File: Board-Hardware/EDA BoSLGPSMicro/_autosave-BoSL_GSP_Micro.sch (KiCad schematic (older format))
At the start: 45 parts, among them CON1 Micro_SD_Card, CON2 BARREL_JACK, IC2 SIM7000, J7 USB_B_Micro, P2 CONN_01X04, P4 CONN_01X04, P7 CONN_01X04, SW1 SPST, U1 MCP1700T-3302E/TT, U2 ATmega328P-AU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

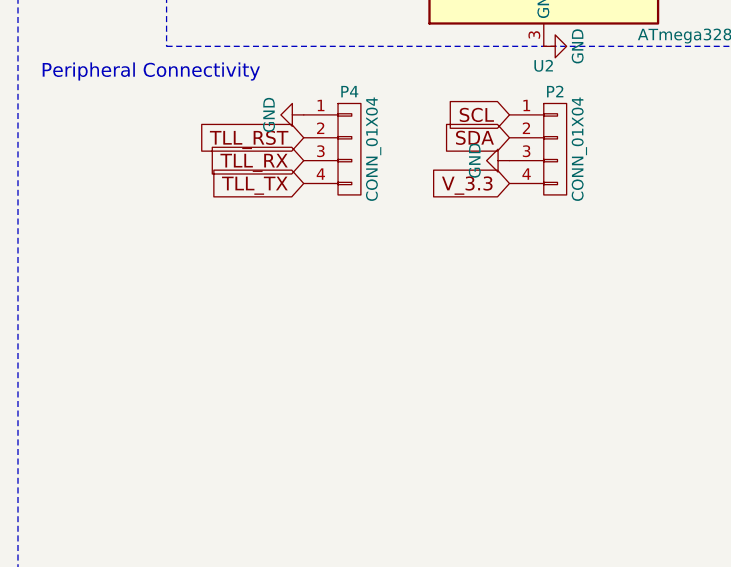
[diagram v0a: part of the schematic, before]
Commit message: added spi header to bosl GPS micro for bootloading
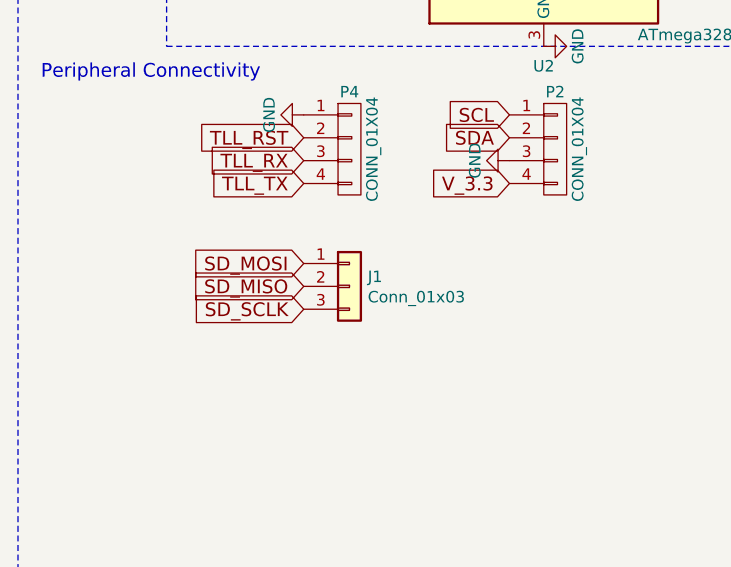
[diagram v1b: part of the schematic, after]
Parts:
- added J1: Conn_01x03, Pin_Headers:Pin_Header_Straight_1x03_Pitch2.54mm, symbol Connector_Generic:Conn_01x03
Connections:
- net SD_MISO: now also J1.2 (Pin_2)
- net SD_MOSI: now also J1.1 (Pin_1)
- net SD_SCLK: now also J1.3 (Pin_3)
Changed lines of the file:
@@
 Text GLabel 2200 4250 0    60   Input ~ 0
 A7
+$Comp
+L Connector_Generic:Conn_01x03 J1
+U 1 1 5DE48010
+P 1950 7700
+F 0 "J1" H 2030 7742 50  0000 L CNN
+F 1 "Conn_01x03" H 2030 7653 50  0000 L CNN
+F 2 "Pin_Headers:Pin_Header_Straight_1x03_Pitch2.54mm" H 1950 7700 50  0001 C CNN
+F 3 "~" H 1950 7700 50  0001 C CNN
+	1    1950 7700
+	1    0    0    -1
+$EndComp
+Text GLabel 1750 7600 0    60   Input ~ 0
+SD_MOSI
+Text GLabel 1750 7700 0    60   Input ~ 0
+SD_MISO
+Text GLabel 1750 7800 0    60   Input ~ 0
+SD_SCLK
 $EndSCHEMATC
